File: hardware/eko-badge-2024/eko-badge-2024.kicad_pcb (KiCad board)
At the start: 2 copper layers, 60 x 121.3 mm, 63 parts, among them J1 UART, J2 Battery, J3 Lentes, J4 OLED, J5 Add-On, J6 Add-On, J7 Battery, P1 USB_C_Plug_USB2.0, Q1 DMG3415U-7, SW1 ON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

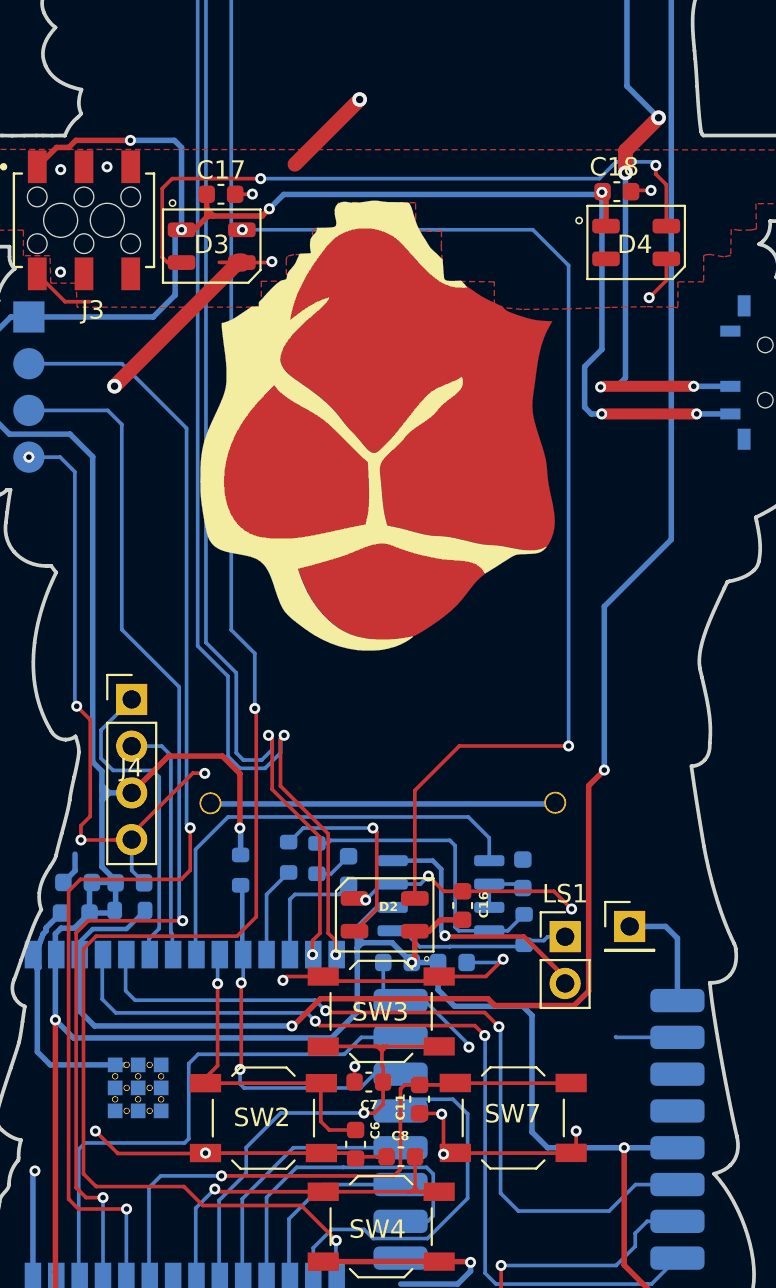
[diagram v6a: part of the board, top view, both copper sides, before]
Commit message: fix(Hw):Moved_Speaker_Connector
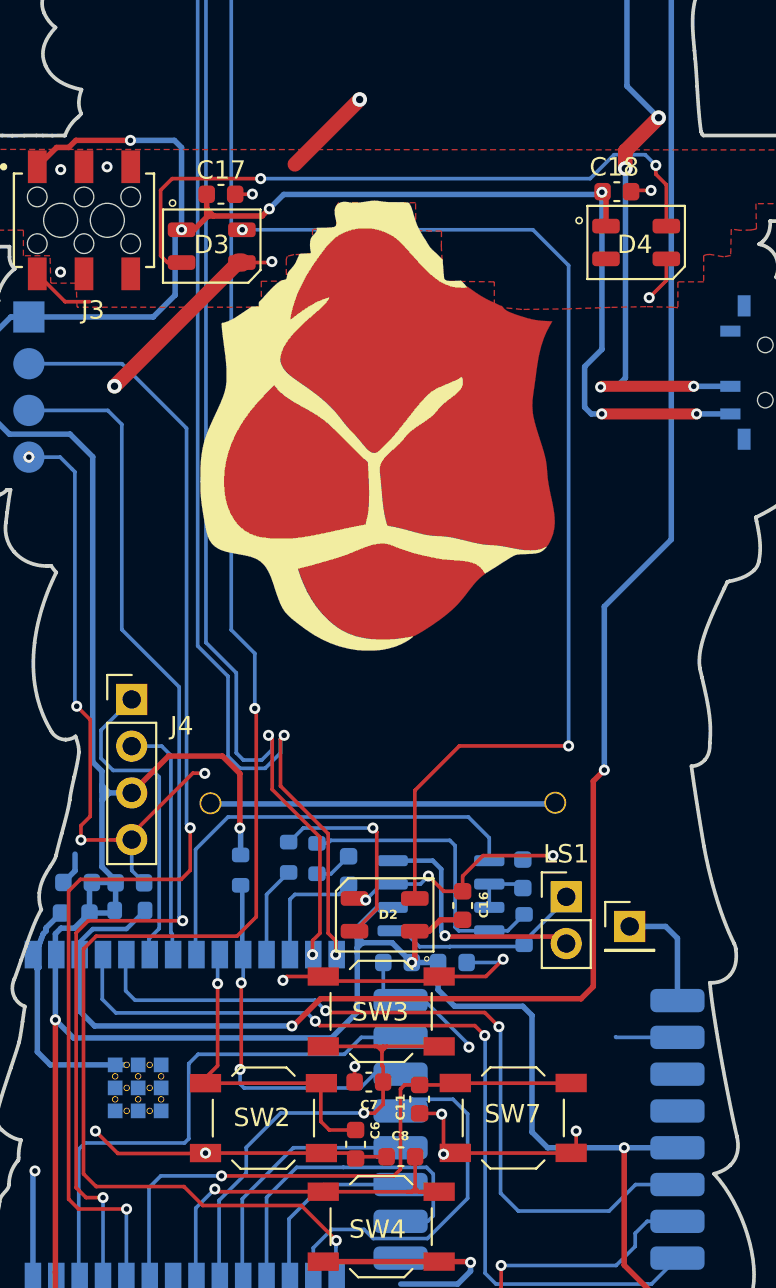
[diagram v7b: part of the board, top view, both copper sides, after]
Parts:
- moved LS1 2.17 mm to (213.4, 107.5)
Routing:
- net GND: track 190.8 -> 189.5 mm
- net Net-(U4-VO+): track 9.96 -> 11.1 mm
- net Net-(U4-VO-): track 14.3 -> 13.3 mm
